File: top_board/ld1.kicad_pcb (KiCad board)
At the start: 2 copper layers, 62 x 81 mm, 45 parts, among them J1 ENCODER, J2 PROG, J3 MISC, J4 POWER, J5 5V, J6 GND, J7 3V3, J8 GPS+OLED, J9 GND, SW3 KLS7-KL-02-N-0-0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

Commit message: Boards done, composition done
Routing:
- net MOSI: track 20.9 -> 24.1 mm
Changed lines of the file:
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@@
 	)
 	(gr_text "R"
-		(at 122.38 91.24 0)
+		(at 122.19 91.18 0)
 		(layer "F.Cu")
 		(effects
@@
 	)
 	(segment
-		(start 129.08 88.6)
-		(end 129.08 66.071878)
-		(width 0.3)
-		(layer "F.Cu")
-		(net 9)
-	)
-	(segment
-		(start 118.496 99.184)
-		(end 129.08 88.6)
-		(width 0.3)
-		(layer "F.Cu")
-		(net 9)
-	)
-	(segment
-		(start 129.08 66.071878)
-		(end 128.58 65.571878)
-		(width 0.3)
-		(layer "F.Cu")
-		(net 9)
-	)
-	(segment
-		(start 128.58 65.571878)
-		(end 128.58 63.39)
-		(width 0.3)
-		(layer "F.Cu")
-		(net 9)
-	)
-	(segment
 		(start 117.196 99.184)
 		(end 118.496 99.184)
@@
 	)
 	(segment
-		(start 128.58 63.39)
-		(end 127.296 62.106)
-		(width 0.3)
-		(layer "F.Cu")
-		(net 9)
-	)
-	(segment
 		(start 127.296 62.106)
 		(end 120.4955 62.106)
@@
 	)
 	(segment
+		(start 118.496 99.184)
+		(end 129.15 88.53)
+		(width 0.3)
+		(layer "F.Cu")
+		(net 9)
+	)
+	(segment
+		(start 128.08 62.89)
+		(end 127.296 62.106)
+		(width 0.3)
+		(layer "F.Cu")
+		(net 9)
+	)
+	(segment
+		(start 129.15 67.16)
+		(end 128.08 66.09)
+		(width 0.3)
+		(layer "F.Cu")
+		(net 9)
+	)
+	(segment
+		(start 129.15 88.53)
+		(end 129.15 67.16)
+		(width 0.3)
+		(layer "F.Cu")
+		(net 9)
+	)
+	(segment
+		(start 128.08 66.09)
+		(end 128.08 62.89)
+		(width 0.3)
+		(layer "F.Cu")
+		(net 9)
+	)
+	(segment
 		(start 100.196 97.914)
 		(end 101.716 97.914)
@@
 	)
 	(segment
+		(start 117.27 81.892894)
+		(end 117.27 75.502894)
+		(width 0.3)
+		(layer "F.Cu")
+		(net 11)
+	)
+	(segment
 		(start 110.09 83.6)
-		(end 110.09 77.29)
+		(end 115.562894 83.6)
 		(width 0.3)
 		(layer "F.Cu")
@@
 	)
 	(segment
-		(start 110.09 77.29)
-		(end 120.194 67.186)
+		(start 120.204 67.186)
+		(end 120.4955 67.186)
 		(width 0.3)
 		(layer "F.Cu")
@@
 	)
 	(segment
-		(start 120.194 67.186)
-		(end 120.4955 67.186)
-		(width 0.3)
-		(layer "F.Cu")
+		(start 117.27 75.502894)
+		(end 118.82 73.952894)
+		(width 0.3)
+		(layer "F.Cu")
+		(net 11)
+	)
+	(segment
+		(start 115.562894 83.6)
+		(end 117.27 81.892894)
+		(width 0.3)
+		(layer "F.Cu")
+		(net 11)
+	)
+	(segment
+		(start 118.82 73.952894)
+		(end 118.82 68.57)
+		(width 0.3)
+		(layer "F.Cu")
+		(net 11)
+	)
+	(segment
+		(start 118.82 68.57)
+		(end 120.204 67.186)
+		(width 0.3)
+		(layer "F.Cu")

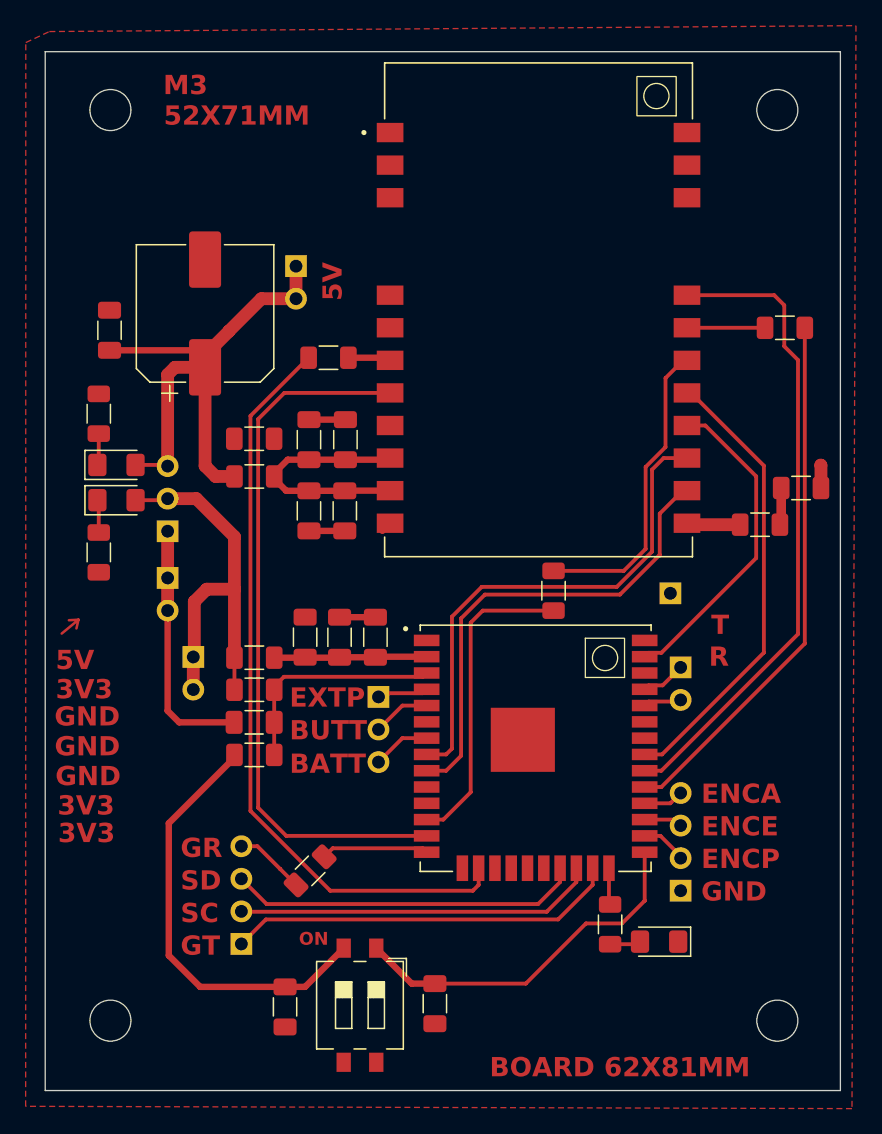
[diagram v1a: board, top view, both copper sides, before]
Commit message: Recovering after git fatal error. Changed M3 to M4
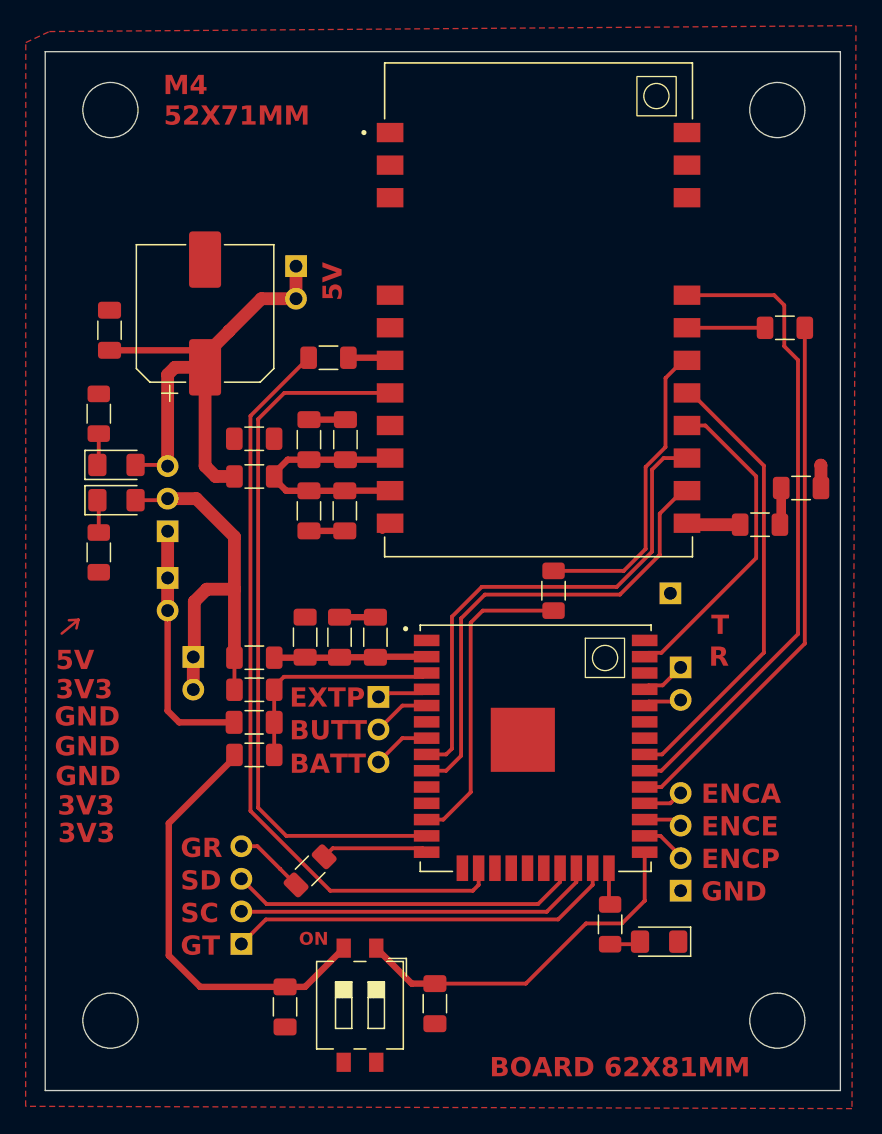
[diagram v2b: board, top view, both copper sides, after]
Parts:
- H1, H2, H3, H4: footprint MountingHole:MountingHole_3.2mm_M3 -> MountingHole:MountingHole_4.3mm_M4
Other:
- board text added: "M4"
- board text removed: "M3"
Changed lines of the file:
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@@
 		)
 	)
-	(footprint "MountingHole:MountingHole_3.2mm_M3"
+	(footprint "MountingHole:MountingHole_4.3mm_M4"
 		(layer "F.Cu")
 		(at 127.54 118.67)
-		(descr "Mounting Hole 3.2mm, no annular, M3")
-		(tags "mounting hole 3.2mm no annular m3")
+		(descr "Mounting Hole 4.3mm, no annular, M4")
+		(tags "mounting hole 4.3mm no annular m4")
 		(property "Reference" "H4"
-			(at 0 -4.2 0)
+			(at 0 -5.3 0)
 			(layer "F.SilkS")
 			(hide yes)
@@
 		)
 		(property "Value" "MountingHole"
-			(at 0 4.2 0)
+			(at 0 5.3 0)
 			(layer "F.Fab")
 			(effects
@@
 			)
 		)
-		(property "Footprint" "MountingHole:MountingHole_3.2mm_M3"
+		(property "Footprint" "MountingHole:MountingHole_4.3mm_M4"
 			(at 0 0 0)
 			(unlocked yes)
@@
 		(fp_circle
 			(center 0 0)
-			(end 3.2 0)
+			(end 4.3 0)
 			(stroke
 				(width 0.15)
@@
 		(fp_circle
 			(center 0 0)
-			(end 3.45 0)
+			(end 4.55 0)
 			(stroke
 				(width 0.05)
@@
 		(pad "" np_thru_hole circle
 			(at 0 0)
-			(size 3.2 3.2)
-			(drill 3.2)
-			(layers "F&B.Cu" "*.Mask")
+			(size 4.3 4.3)
+			(drill 4.3)
+			(layers "*.Cu" "*.Mask")
 		)
 	)
@@
 		)
 	)
-	(footprint "MountingHole:MountingHole_3.2mm_M3"
+	(footprint "MountingHole:MountingHole_4.3mm_M4"
 		(layer "F.Cu")
 		(at 75.54 47.67)
-		(descr "Mounting Hole 3.2mm, no annular, M3")
-		(tags "mounting hole 3.2mm no annular m3")
+		(descr "Mounting Hole 4.3mm, no annular, M4")
+		(tags "mounting hole 4.3mm no annular m4")
 		(property "Reference" "H1"
-			(at 0 -4.2 0)
+			(at 0 -5.3 0)
 			(layer "F.SilkS")
 			(hide yes)
@@
 		)
 		(property "Value" "MountingHole"
-			(at 0 4.2 0)
+			(at 0 5.3 0)
 			(layer "F.Fab")
 			(effects
@@
 			)
 		)
-		(property "Footprint" "MountingHole:MountingHole_3.2mm_M3"
+		(property "Footprint" "MountingHole:MountingHole_4.3mm_M4"
 			(at 0 0 0)
 			(unlocked yes)
@@
 		(fp_circle
 			(center 0 0)
-			(end 3.2 0)
+			(end 4.3 0)
 			(stroke
 				(width 0.15)
@@
 		(fp_circle
 			(center 0 0)
-			(end 3.45 0)
+			(end 4.55 0)
 			(stroke
 				(width 0.05)
@@
 		(pad "" np_thru_hole circle
 			(at 0 0)
-			(size 3.2 3.2)
-			(drill 3.2)
+			(size 4.3 4.3)
+			(drill 4.3)
 			(layers "*.Cu" "*.Mask")
 		)
@@
 		)
 	)
-	(footprint "MountingHole:MountingHole_3.2mm_M3"
+	(footprint "MountingHole:MountingHole_4.3mm_M4"
 		(layer "F.Cu")
 		(at 127.54 47.67)
-		(descr "Mounting Hole 3.2mm, no annular, M3")
-		(tags "mounting hole 3.2mm no annular m3")
+		(descr "Mounting Hole 4.3mm, no annular, M4")
+		(tags "mounting hole 4.3mm no annular m4")
 		(property "Reference" "H2"
-			(at 0 -4.2 0)
+			(at 0 -5.3 0)
 			(layer "F.SilkS")
 			(hide yes)
@@
 		)
 		(property "Value" "MountingHole"
-			(at 0 4.2 0)
+			(at 0 5.3 0)
 			(layer "F.Fab")
 			(effects
@@
 			)
 		)
-		(property "Footprint" "MountingHole:MountingHole_3.2mm_M3"
+		(property "Footprint" "MountingHole:MountingHole_4.3mm_M4"
 			(at 0 0 0)
 			(unlocked yes)
@@
 		(fp_circle
 			(center 0 0)
-			(end 3.2 0)
+			(end 4.3 0)
 			(stroke
 				(width 0.15)
@@
 		(fp_circle
 			(center 0 0)
-			(end 3.45 0)
+			(end 4.55 0)
 			(stroke
 				(width 0.05)
@@
 		(pad "" np_thru_hole circle
 			(at 0 0)
-			(size 3.2 3.2)
-			(drill 3.2)
+			(size 4.3 4.3)
+			(drill 4.3)
 			(layers "*.Cu" "*.Mask")
 		)
@@
 		)
 	)
-	(footprint "MountingHole:MountingHole_3.2mm_M3"
+	(footprint "MountingHole:MountingHole_4.3mm_M4"
 		(layer "F.Cu")
 		(at 75.54 118.67)
-		(descr "Mounting Hole 3.2mm, no annular, M3")
-		(tags "mounting hole 3.2mm no annular m3")
+		(descr "Mounting Hole 4.3mm, no annular, M4")
+		(tags "mounting hole 4.3mm no annular m4")
 		(property "Reference" "H3"
-			(at 0 -4.2 0)
+			(at 0 -5.3 0)
 			(layer "F.SilkS")
 			(hide yes)
@@
 		)
 		(property "Value" "MountingHole"
-			(at 0 4.2 0)
+			(at 0 5.3 0)
 			(layer "F.Fab")
 			(effects
@@
 			)
 		)
-		(property "Footprint" "MountingHole:MountingHole_3.2mm_M3"
+		(property "Footprint" "MountingHole:MountingHole_4.3mm_M4"
 			(at 0 0 0)
 			(unlocked yes)
@@
 		(fp_circle
 			(center 0 0)
-			(end 3.2 0)
+			(end 4.3 0)
 			(stroke
 				(width 0.15)
@@
 		(fp_circle
 			(center 0 0)
-			(end 3.45 0)
+			(end 4.55 0)
 			(stroke
 				(width 0.05)
@@
 		(pad "" np_thru_hole circle
 			(at 0 0)
-			(size 3.2 3.2)
-			(drill 3.2)
+			(size 4.3 4.3)
+			(drill 4.3)
 			(layers "*.Cu" "*.Mask")
 		)
@@
 		)
 	)
-	(gr_text "M3"
+	(gr_text "M4"
 		(at 79.65 46.61 0)
 		(layer "F.Cu")
